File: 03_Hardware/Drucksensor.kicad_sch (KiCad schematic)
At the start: 101 parts, among them J110 DS18B20, J111 Conn_01x06_Male, SW103 SW_DIP_x08, U103 ATmega8A-A, U104 REF3040, U105 74HC165, U107 SN75176AD, U108 CAT24M01W, Y101 16MHz

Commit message: I2C Pullups hinzugefügt
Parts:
- added ? (x2): (no value), symbol Device:Fuse
- added R127 (x2): 100k, symbol Device:R
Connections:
- net +24V: now also ?.1; no longer JP101.1 (A)
- net +3V3: now also R127.2, R127.2
- net +5V: now also ?.1; no longer JP101.1 (A)
- net I2C_SCL: now also R127.1
- net I2C_SDA: now also R127.1
- new net: ?.2, JP101.1 (A) (x2)
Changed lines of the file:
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@@
     (effects (font (size 1.27 1.27)) (justify right bottom))
   )
+  (label "I2C_SCL" (at 250.19 210.82 270) (fields_autoplaced)
+    (effects (font (size 1.27 1.27)) (justify right bottom))
+  )
   (label "Tacho" (at 260.35 332.74 180) (fields_autoplaced)
     (effects (font (size 1.27 1.27)) (justify right bottom))
@@
     (effects (font (size 1.27 1.27)) (justify left bottom))
   )
+  (label "I2C_SDA" (at 237.49 210.82 270) (fields_autoplaced)
+    (effects (font (size 1.27 1.27)) (justify right bottom))
+  )
   (label "TX_2" (at 196.85 341.63 0) (fields_autoplaced)
     (effects (font (size 1.27 1.27)) (justify left bottom))
@@
     (pin "1")
   )
+  (symbol (lib_id "Device:R") (at 237.49 207.01 180) (unit 1)
+    (in_bom yes) (on_board yes) (dnp no) (fields_autoplaced)
+    (default_instance (reference "R127") (unit 1) (value "100k") (footprint ""))
+    (property "Reference" "R127" (id 0) (at 240.03 206.375 0)
+      (effects (font (size 1.27 1.27)) (justify right))
+    )
+    (property "Value" "100k" (id 1) (at 240.03 208.915 0)
+      (effects (font (size 1.27 1.27)) (justify right))
+    )
+    (property "Footprint" "" (id 2) (at 239.268 207.01 90)
+      (effects (font (size 1.27 1.27)) hide)
+    )
+    (property "Datasheet" "~" (id 3) (at 237.49 207.01 0)
+      (effects (font (size 1.27 1.27)) hide)
+    )
+    (pin "1")
+    (pin "2")
+  )
   (symbol (lib_id "power:PWR_FLAG") (at 381 237.49 0) (mirror x) (unit 1)
     (in_bom yes) (on_board yes) (dnp no)
@@
     (pin "2")
   )
+  (symbol (lib_id "Device:Fuse") (at 336.55 170.18 90) (mirror x) (unit 1)
+    (in_bom yes) (on_board yes) (dnp no) (fields_autoplaced)
+    (default_instance (reference "") (unit 1) (value "") (footprint ""))
+    (property "Reference" "" (id 0) (at 336.55 165.1 90)
+      (effects (font (size 1.27 1.27)))
+    )
+    (property "Value" "" (id 1) (at 336.55 167.64 90)
+      (effects (font (size 1.27 1.27)))
+    )
+    (property "Footprint" "" (id 2) (at 336.55 168.402 90)
+      (effects (font (size 1.27 1.27)) hide)
+    )
+    (property "Datasheet" "~" (id 3) (at 336.55 170.18 0)
+      (effects (font (size 1.27 1.27)) hide)
+    )
+    (pin "1")
+    (pin "2")
+  )
   (symbol (lib_id "power:VAA") (at 181.61 194.31 0) (unit 1)
     (in_bom yes) (on_board yes) (dnp no)
@@
     (pin "2")
   )
-  (symbol (lib_id "power:+24V") (at 340.36 157.48 90) (unit 1)
+  (symbol (lib_id "Device:R") (at 250.19 207.01 180) (unit 1)
+    (in_bom yes) (on_board yes) (dnp no) (fields_autoplaced)
+    (default_instance (reference "R127") (unit 1) (value "100k") (footprint ""))
+    (property "Reference" "R127" (id 0) (at 252.73 206.375 0)
+      (effects (font (size 1.27 1.27)) (justify right))
+    )
+    (property "Value" "100k" (id 1) (at 252.73 208.915 0)
+      (effects (font (size 1.27 1.27)) (justify right))
+    )
+    (property "Footprint" "" (id 2) (at 251.968 207.01 90)
+      (effects (font (size 1.27 1.27)) hide)
+    )
+    (property "Datasheet" "~" (id 3) (at 250.19 207.01 0)
+      (effects (font (size 1.27 1.27)) hide)
+    )
+    (pin "1")
+    (pin "2")
+  )
+  (symbol (lib_id "power:+24V") (at 332.74 157.48 90) (unit 1)
     (in_bom yes) (on_board yes) (dnp no) (fields_autoplaced)
     (default_instance (reference "#PWR?") (unit 1) (value "+24V") (footprint ""))
-    (property "Reference" "#PWR?" (id 0) (at 344.17 157.48 0)
+    (property "Reference" "#PWR?" (id 0) (at 336.55 157.48 0)
       (effects (font (size 1.27 1.27)) hide)
     )
-    (property "Value" "+24V" (id 1) (at 336.55 158.115 90)
+    (property "Value" "+24V" (id 1) (at 328.93 158.115 90)
       (effects (font (size 1.27 1.27)) (justify left))
     )
-    (property "Footprint" "" (id 2) (at 340.36 157.48 0)
+    (property "Footprint" "" (id 2) (at 332.74 157.48 0)
       (effects (font (size 1.27 1.27)) hide)
     )
-    (property "Datasheet" "" (id 3) (at 340.36 157.48 0)
+    (property "Datasheet" "" (id 3) (at 332.74 157.48 0)
       (effects (font (size 1.27 1.27)) hide)
     )
@@
     (pin "1")
   )
-  (symbol (lib_id "power:+5V") (at 340.36 170.18 90) (mirror x) (unit 1)
+  (symbol (lib_id "power:+5V") (at 332.74 170.18 90) (mirror x) (unit 1)
     (in_bom yes) (on_board yes) (dnp no)
     (default_instance (reference "") (unit 1) (value "") (footprint ""))
-    (property "Reference" "" (id 0) (at 344.17 170.18 0)
+    (property "Reference" "" (id 0) (at 336.55 170.18 0)
       (effects (font (size 1.27 1.27)) hide)
     )
-    (property "Value" "" (id 1) (at 337.1849 170.5483 90)
+    (property "Value" "" (id 1) (at 329.5649 170.5483 90)
       (effects (font (size 1.27 1.27)) (justify left))
     )
-    (property "Footprint" "" (id 2) (at 340.36 170.18 0)
+    (property "Footprint" "" (id 2) (at 332.74 170.18 0)
       (effects (font (size 1.27 1.27)) hide)
     )
-    (property "Datasheet" "" (id 3) (at 340.36 170.18 0)
+    (property "Datasheet" "" (id 3) (at 332.74 170.18 0)
       (effects (font (size 1.27 1.27)) hide)
     )
@@
     (pin "2")
   )
+  (symbol (lib_id "power:+3.3V") (at 250.19 203.2 0) (unit 1)
+    (in_bom yes) (on_board yes) (dnp no)
+    (default_instance (reference "#PWR?") (unit 1) (value "+3.3V") (footprint ""))
+    (property "Reference" "#PWR?" (id 0) (at 250.19 207.01 0)
+      (effects (font (size 1.27 1.27)) hide)
+    )
+    (property "Value" "+3.3V" (id 1) (at 250.19 199.39 90)
+      (effects (font (size 1.27 1.27)) (justify left))
+    )
+    (property "Footprint" "" (id 2) (at 250.19 203.2 0)
+      (effects (font (size 1.27 1.27)) hide)
+    )
+    (property "Datasheet" "" (id 3) (at 250.19 203.2 0)
+      (effects (font (size 1.27 1.27)) hide)
+    )
+    (pin "1")
+  )
   (symbol (lib_id "Device:R") (at 140.97 201.93 90) (unit 1)
     (in_bom yes) (on_board yes) (dnp no)
@@
     (pin "1")
   )
+  (symbol (lib_id "Device:Fuse") (at 336.55 157.48 90) (mirror x) (unit 1)
+    (in_bom yes) (on_board yes) (dnp no) (fields_autoplaced)
+    (default_instance (reference "") (unit 1) (value "") (footprint ""))
+    (property "Reference" "" (id 0) (at 336.55 152.4 90)
+      (effects (font (size 1.27 1.27)))
+    )
+    (property "Value" "" (id 1) (at 336.55 154.94 90)
+      (effects (font (size 1.27 1.27)))
+    )
+    (property "Footprint" "" (id 2) (at 336.55 155.702 90)
+      (effects (font (size 1.27 1.27)) hide)
+    )
+    (property "Datasheet" "~" (id 3) (at 336.55 157.48 0)
+      (effects (font (size 1.27 1.27)) hide)
+    )
+    (pin "1")
+    (pin "2")
+  )
   (symbol (lib_id "Device:R") (at 260.35 119.38 0) (mirror x) (unit 1)
     (in_bom yes) (on_board yes) (dnp no) (fields_autoplaced)
@@
     (pin "2")
   )
+  (symbol (lib_id "power:+3.3V") (at 237.49 203.2 0) (unit 1)
+    (in_bom yes) (on_board yes) (dnp no)
+    (default_instance (reference "#PWR?") (unit 1) (value "+3.3V") (footprint ""))
+    (property "Reference" "#PWR?" (id 0) (at 237.49 207.01 0)
+      (effects (font (size 1.27 1.27)) hide)
+    )
+    (property "Value" "+3.3V" (id 1) (at 237.49 199.39 90)
+      (effects (font (size 1.27 1.27)) (justify left))
+    )
+    (property "Footprint" "" (id 2) (at 237.49 203.2 0)
+      (effects (font (size 1.27 1.27)) hide)
+    )
+    (property "Datasheet" "" (id 3) (at 237.49 203.2 0)
+      (effects (font (size 1.27 1.27)) hide)
+    )
+    (pin "1")
+  )
   (symbol (lib_id "power:GND") (at 287.02 200.66 0) (mirror y) (unit 1)
     (in_bom yes) (on_board yes) (dnp no) (fields_autoplaced)
@@
       (reference "#PWR?") (unit 1) (value "GNDA") (footprint "")
     )
+    (path "/6568fd68-7a16-4e2c-9d0e-eb0a52707066"
+      (reference "#PWR?") (unit 1) (value "+3.3V") (footprint "")
+    )
     (path "/b13d1e4e-9552-4848-9d7d-63571c3c163b"
       (reference "#PWR?") (unit 1) (value "GNDA") (footprint "")
@@
       (reference "#PWR?") (unit 1) (value "GNDA") (footprint "")
     )
+    (path "/f935f892-23cb-48cb-9892-9c04d4931eb5"
+      (reference "#PWR?") (unit 1) (value "+3.3V") (footprint "")
+    )
     (path "/88276ede-ec0f-4f9f-9998-4699edeb1bbe"
       (reference "A101") (unit 1) (value "Arduino_UNO_R3") (footprint "Module:Arduino_UNO_R3")
@@
       (reference "F102") (unit 1) (value "Fuse") (footprint "Resistor_SMD:R_1210_3225Metric")
     )
+    (path "/8e3c3b2e-52de-4ebb-90ec-c1aaccc78227"
+      (reference "F103") (unit 1) (value "Fuse") (footprint "Resistor_SMD:R_1210_3225Metric")
+    )
+    (path "/0aa730a8-c48e-4a15-92b6-771da6022fe8"
+      (reference "F104") (unit 1) (value "Fuse") (footprint "Resistor_SMD:R_1210_3225Metric")
+    )
     (path "/973b7866-c1ee-4ab1-b496-96ae751196af"
       (reference "J101") (unit 1) (value "24V in") (footprint "Connector_JST:JST_XH_B2B-XH-A_1x02_P2.50mm_Vertical")
@@
       (reference "R134") (unit 1) (value "tbd") (footprint "")
     )
+    (path "/07bcf103-baac-410f-81b6-b4d45ac69420"
+      (reference "R135") (unit 1) (value "4,7k") (footprint "")
+    )
+    (path "/0de11044-7923-43e0-9e87-2a46660c03b9"
+      (reference "R136") (unit 1) (value "4,7k") (footprint "")
+    )
     (path "/e866e4e7-fc02-45db-8eda-86cbe5657b80/a0d7e60e-8589-4c41-aed7-7c42a7981bc4"

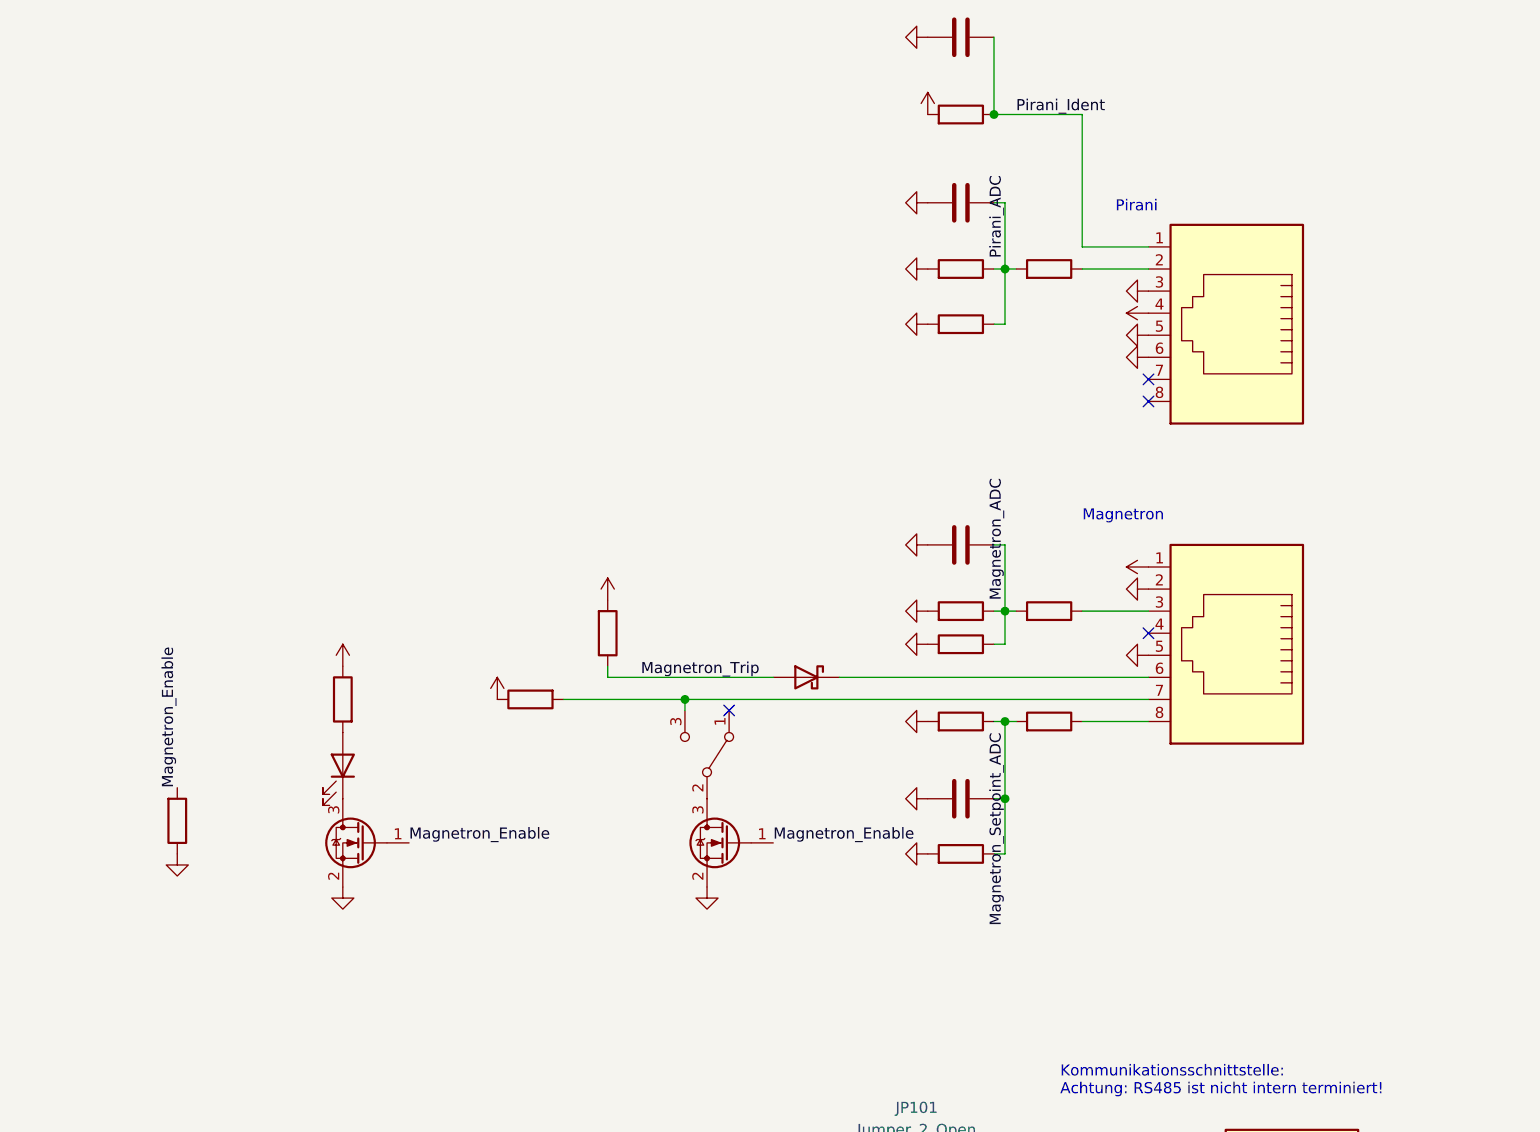
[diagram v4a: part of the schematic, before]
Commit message: Röhreneingänge angelegt
Messröhren sind jetzt mit Edwards-Gängiger Beschaltung angelegt.
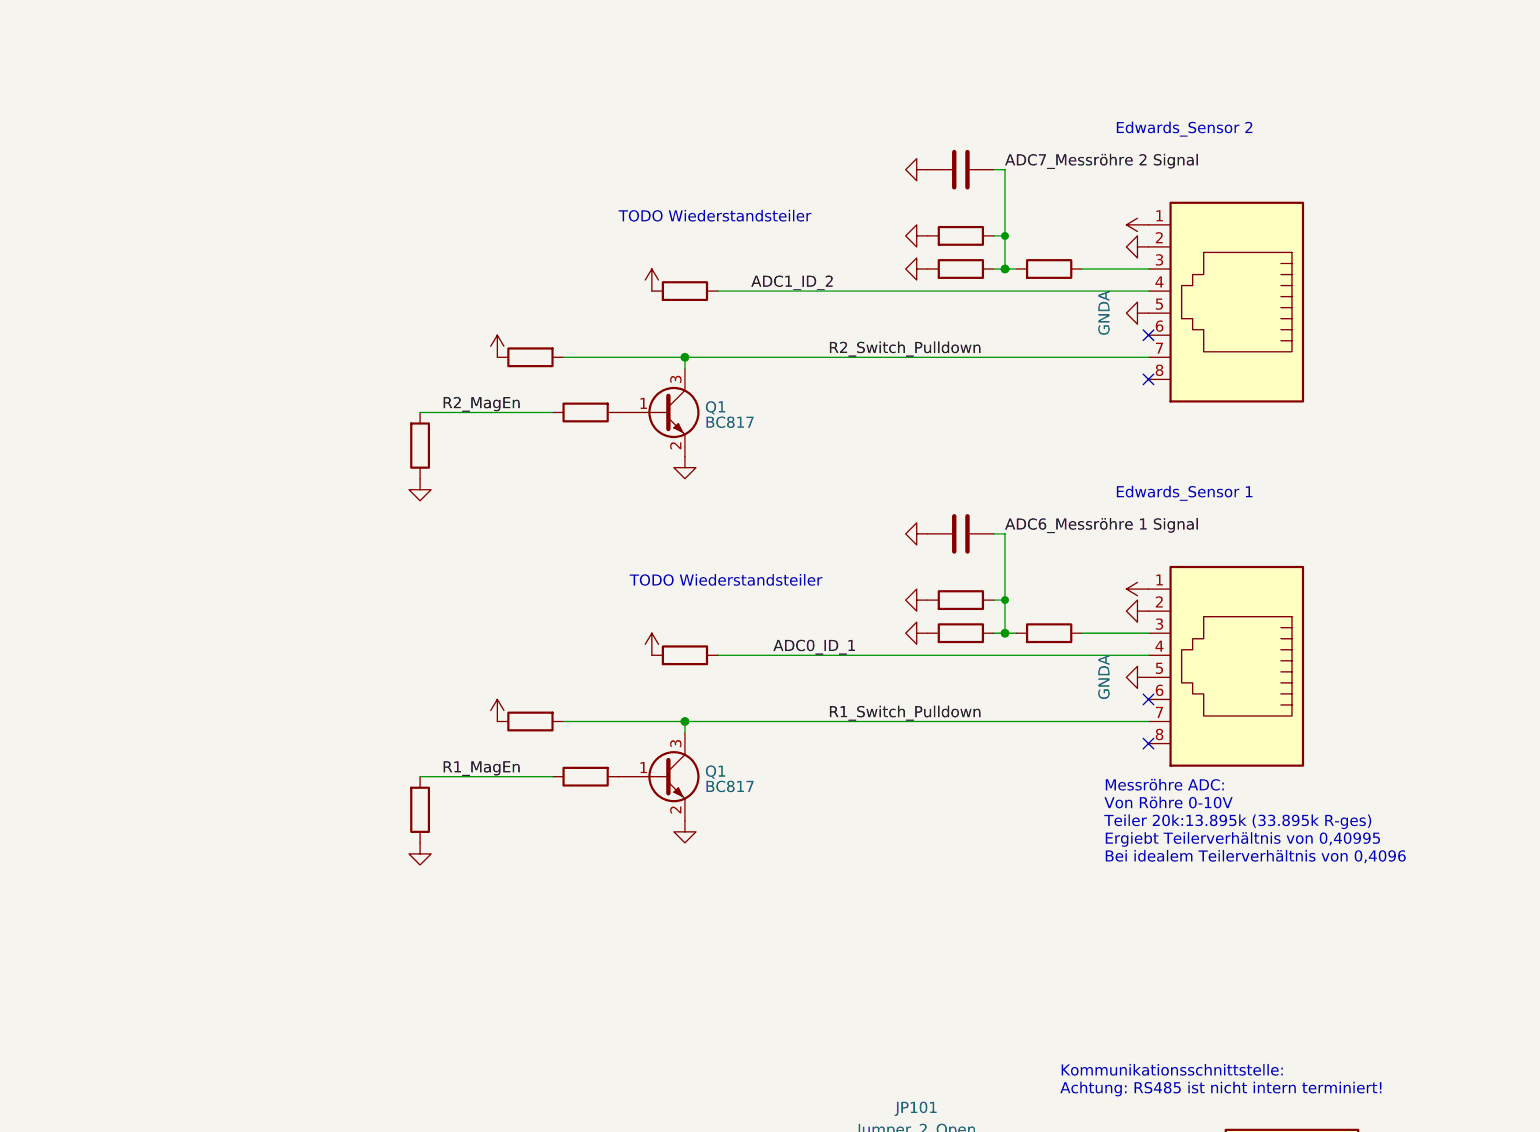
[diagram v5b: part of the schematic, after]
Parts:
- removed ? (x14): (no value), symbol Device:R
- removed ? (x4): (no value), symbol Device:C
- removed ? (x2): (no value), symbol Device:Q_NMOS_GSD
- removed ?: (no value), symbol Device:LED
- removed ?: (no value), symbol Device:D_Schottky
- removed ? (x2): (no value), symbol Connector:RJ45
- removed ?: (no value), symbol Switch:SW_SPDT
- added ? (x14): (no value), symbol Device:R
- added ? (x2): (no value), symbol Connector:RJ45
- added ? (x2): (no value), symbol Device:C
- added Q1 (x2): BC817, Package_TO_SOT_SMD:SOT-23, symbol Transistor_BJT:BC817
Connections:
- net +24V: now also ?.1, ?.1, ?.1, ?.1
- net +5V: now also ?.2, ?.2
- net ADC0_ID_1: now also ?.1, ?.4
- net ADC1_ID_2: now also ?.1, ?.4
- net ADC6_Messröhre 1 Signal: now also ?.1, ?.1, ?.1, ?.2
- net ADC7_Messröhre 2 Signal: now also ?.1, ?.1, ?.1, ?.2
- net GND: now also ?.1, ?.1, ?.2, ?.2, ?.2, ?.2, ?.2, ?.2, ?.2, ?.2, Q1.2 (E), Q1.2 (E)
- net GNDA: now also ?.5, ?.5
- net R1_MagEn: now also ?.1, ?.2
- net R2_MagEn: now also ?.1, ?.2
- new net: ?.2, Q1.1 (B) (x2)
- new net: ?.1, ?.3 (x2)
- new net R1_Switch_Pulldown: ?.2, ?.7, Q1.3 (C)
- new net R2_Switch_Pulldown: ?.2, ?.7, Q1.3 (C)
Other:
- note added: "Edwards_Sensor 1"
- note added: "Edwards_Sensor 2"
- note added: "Messröhre ADC: Von Röhre 0-10V Teiler 20k:13.895k (33.895k R-ges) Ergiebt Teilerverhältnis von 0,40995 Bei idealem Teilerverhältnis von 0,4096"
- note added: "TODO Wiederstandsteiler"
- note removed: "Magnetron"
- note removed: "Pirani"
